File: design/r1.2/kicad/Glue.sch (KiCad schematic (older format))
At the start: 32 parts, among them IC2 ATF16V8BQL-15PU, IC3 ATF16V8BQL, IC5 ATF16V8BQL, IC6 74174N, IC8 555N, IC9 74LS01N, Q2 5H8ET-10.000, Q3 5H8ET-4.000

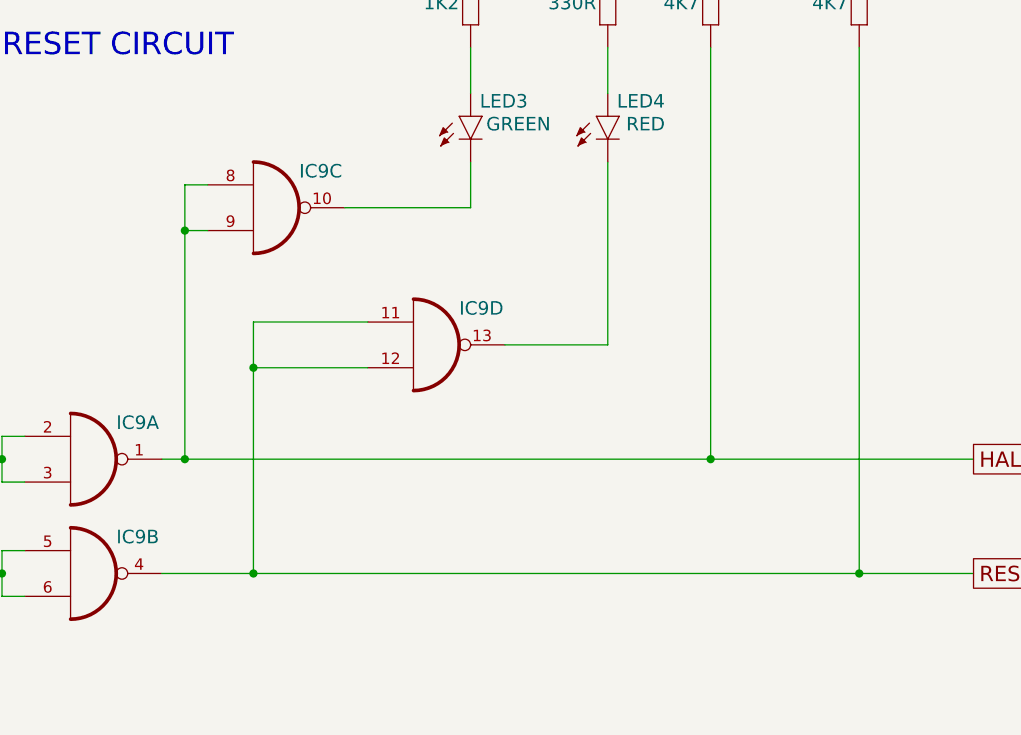
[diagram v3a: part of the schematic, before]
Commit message: Fix reset LED snafu
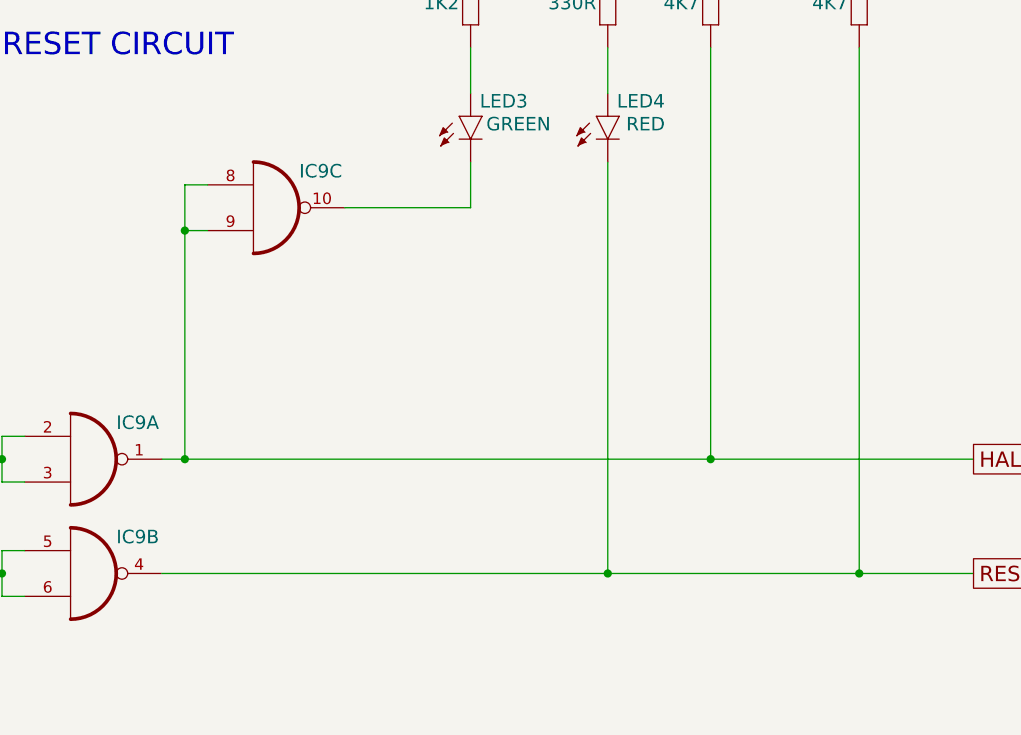
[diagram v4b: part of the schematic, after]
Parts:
- removed unit 4 of IC9
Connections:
- net RESET: now also LED3.K (C)
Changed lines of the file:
@@
 Text GLabel 3750 8500 3    70   UnSpc ~ 0
 IPL2
-$Comp
-L rosco_m68k-eagle-import:7401N IC?
-U 4 1 5ED1F8C3
-P 14000 8000
-AR Path="/5ED1F8C3" Ref="IC?"  Part="3"
-AR Path="/5E53B952/5ED1F8C3" Ref="IC9"  Part="4"
-F 0 "IC9" H 14100 8125 59  0000 L BNN
-F 1 "74LS01N" H 14100 7800 59  0001 L BNN
-F 2 "rosco_m68k:DIL14" H 14000 8000 50  0001 C CNN
-F 3 "" H 14000 8000 50  0001 C CNN
-	4    14000 8000
-	1    0    0    -1
-$EndComp
 Wire Wire Line
 	12900 7500 12900 8500
@@
 	12900 8500 15200 8500
 Connection ~ 12900 8500
-Wire Wire Line
-	12800 9000 13200 9000
-Wire Wire Line
-	13200 7900 13200 8100
-Connection ~ 13200 9000
-Connection ~ 13200 8100
-Wire Wire Line
-	13200 8100 13200 9000
-Wire Wire Line
-	14750 7200 14750 8000
-Wire Wire Line
-	13200 7900 13700 7900
-Wire Wire Line
-	13200 8100 13700 8100
-Wire Wire Line
-	14300 8000 14750 8000
 Connection ~ 15850 9000
 Wire Wire Line
 	15850 9000 16350 9000
-Wire Wire Line
-	13200 9000 15850 9000
 Wire Wire Line
 	15200 6200 15850 6200
@@
 A17
 Wire Wire Line
+	12800 9000 14750 9000
+Wire Wire Line
+	14750 7200 14750 9000
+Wire Wire Line
 	18700 6600 19700 6600
 Wire Bus Line
@@
 Wire Bus Line
 	19400 6050 19400 7500
+Connection ~ 14750 9000
+Wire Wire Line
+	14750 9000 15850 9000
 $EndSCHEMATC

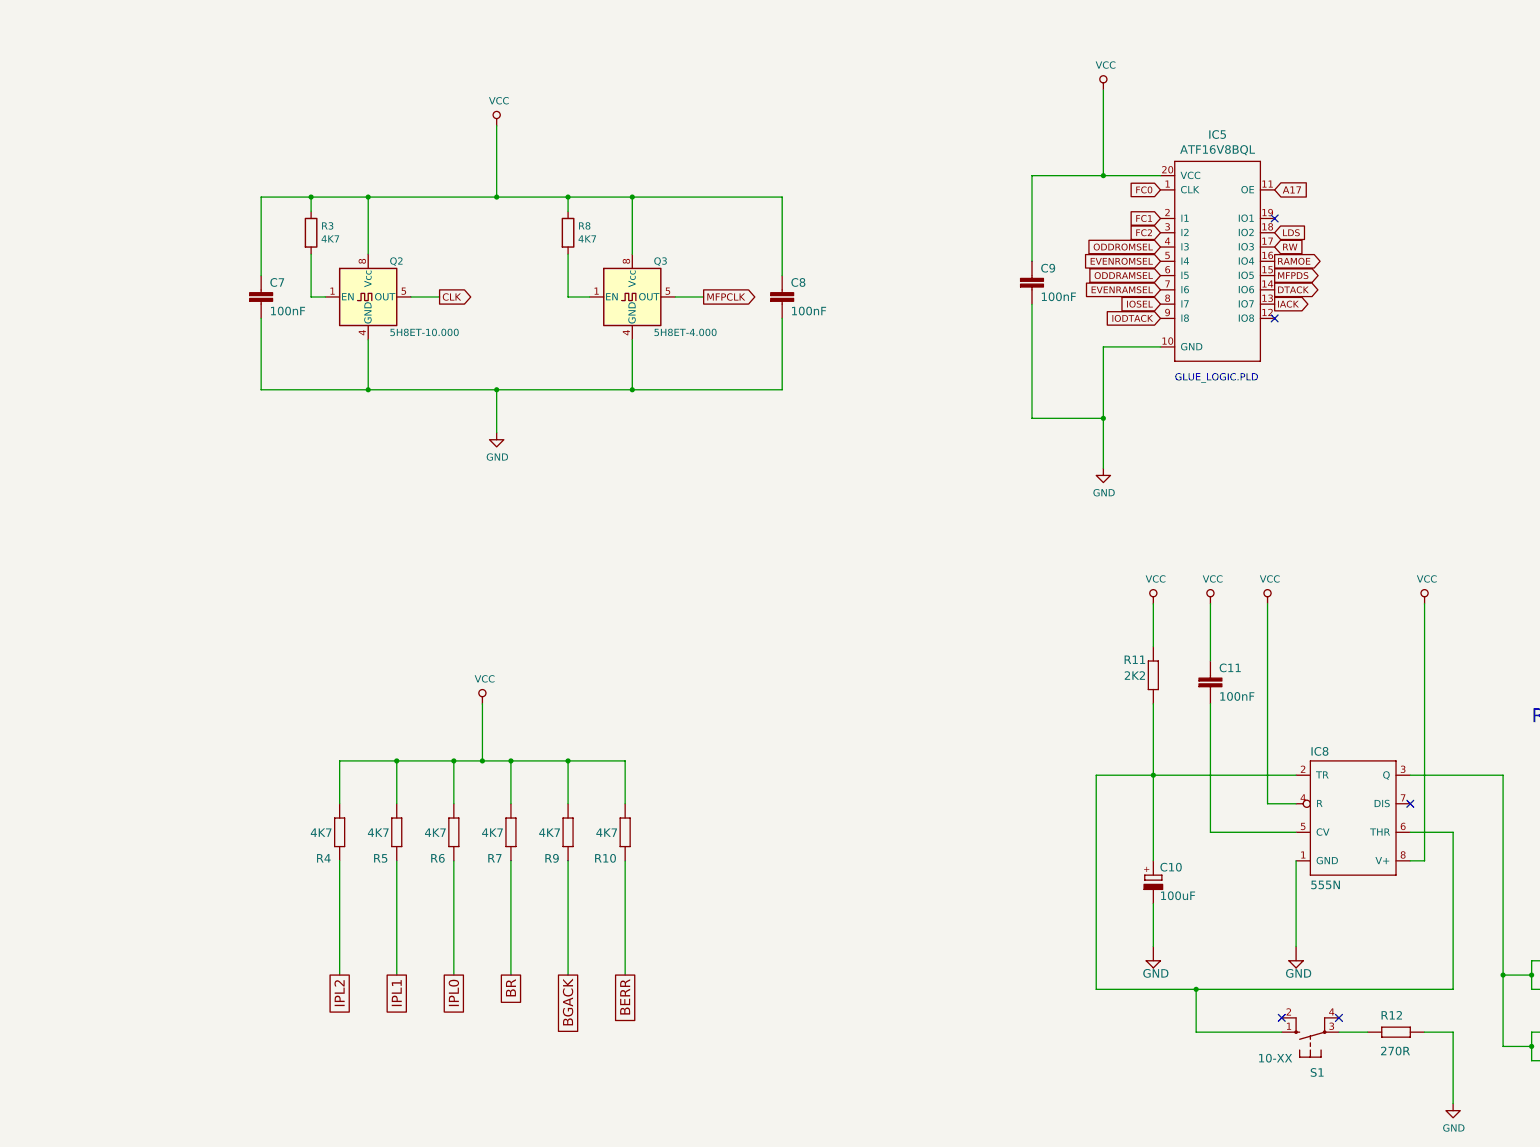
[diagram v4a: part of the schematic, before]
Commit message: Add DTACK watchdog, tidy up footprints
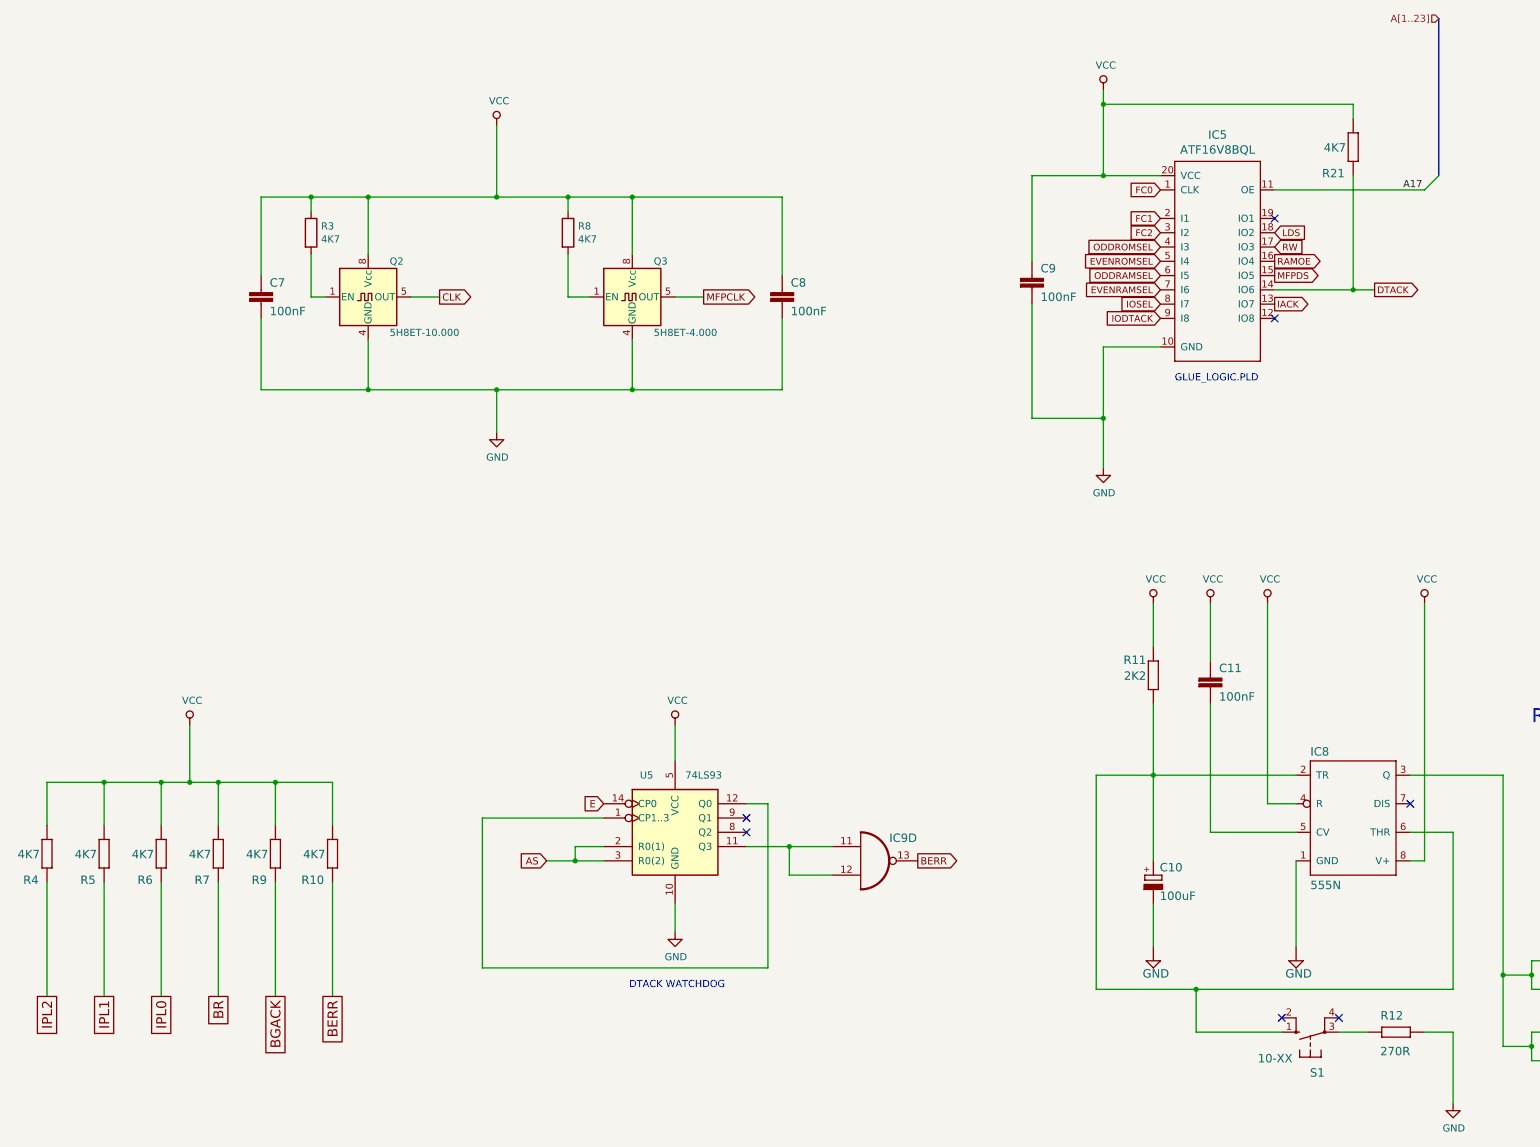
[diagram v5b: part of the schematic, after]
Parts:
- added unit 4 of IC9
- added R21: 4K7, rosco_m68k:0207_10, symbol rosco_m68k-eagle-import:R-EU_0207_10
- added U5: 74LS93, Package_DIP:DIP-14_W7.62mm_Socket_LongPads, symbol 74xx:74LS93
- IC6: footprint rosco_m68k:DIL16 -> Package_DIP:DIP-16_W7.62mm_Socket_LongPads
- IC9: footprint rosco_m68k:DIL14 -> Package_DIP:DIP-14_W7.62mm_Socket_LongPads
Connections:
- net AS: now also U5.2 (R0(1)), U5.3 (R0(2))
- net BERR: now also IC9.13 (O)
- net DTACK: now also R21.1
- net GND: now also U5.10 (GND)
- net VCC: now also R21.2, U5.5 (VCC)
- new net: U5.1 (CP1..3), U5.12 (Q0)
- new net: IC9.11 (I0), IC9.12 (I1), U5.11 (Q3)
- new net E: U5.14 (CP0)
- no-connect marks 10 -> 12
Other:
- note added: "DTACK WATCHDOG"
- moved on the sheet: R10, R4, R5, R6, R7, R9

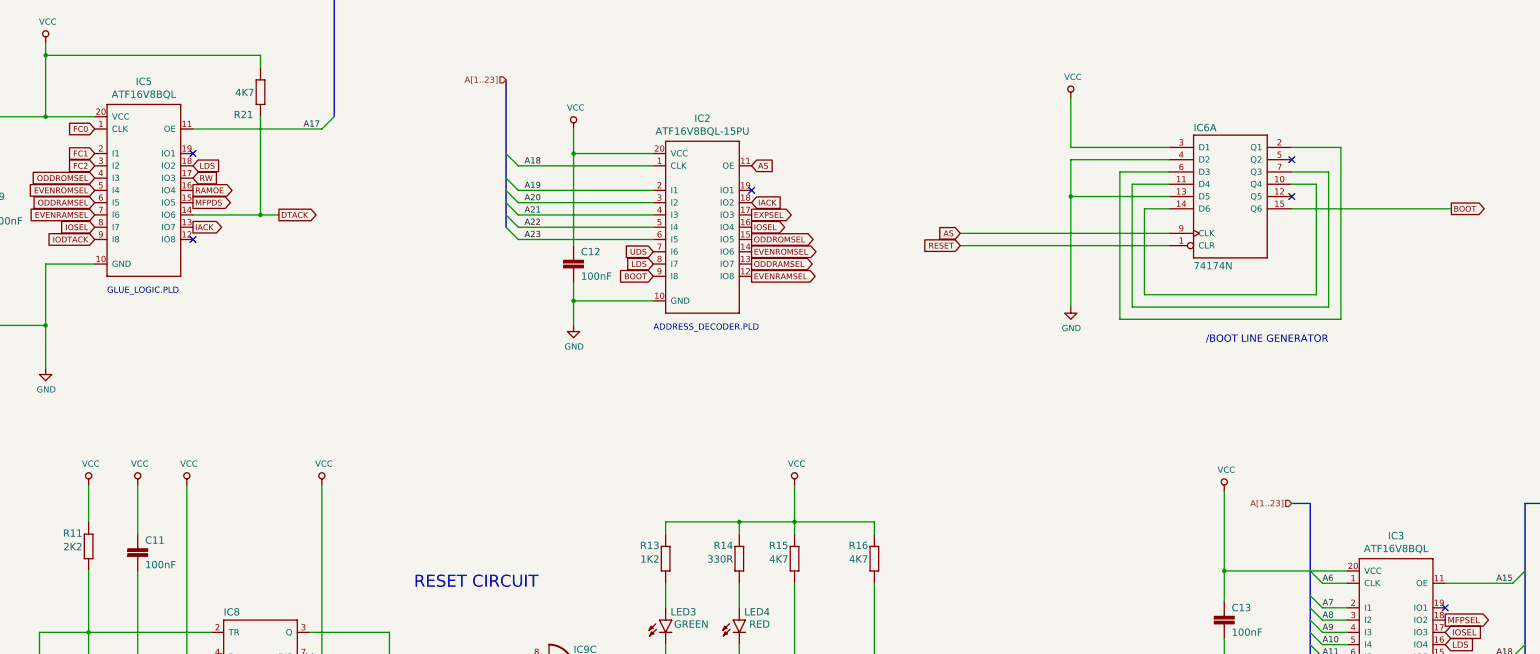
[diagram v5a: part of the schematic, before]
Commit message: Rerate LED limiters for new LED stock
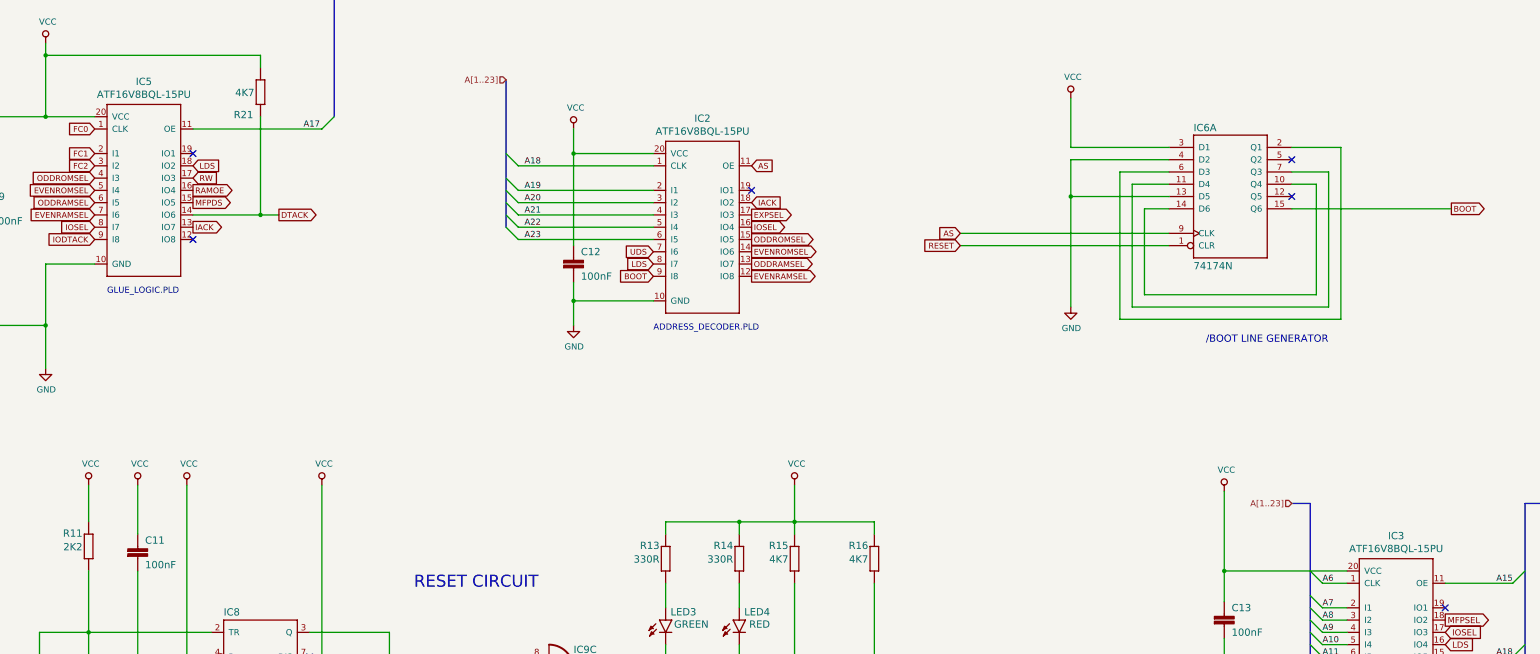
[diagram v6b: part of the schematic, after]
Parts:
- IC3, IC5: value ATF16V8BQL -> ATF16V8BQL-15PU
- R15: value 1K2 -> 330R
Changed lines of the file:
@@
 AR Path="/5E53B952/FD2CBBBB" Ref="R13"  Part="1"
 F 0 "R13" V 14291 6550 59  0000 L BNN
-F 1 "1K2" V 14180 6550 59  0000 L BNN
+F 1 "330R" V 14180 6550 59  0000 L BNN
 F 2 "rosco_m68k:0207_10" H 14150 6500 50  0001 C CNN
 F 3 "" H 14150 6500 50  0001 C CNN
@@
 AR Path="/5E53B952/5EE7D485" Ref="IC5"  Part="1"
 F 0 "IC5" H 9900 4386 59  0000 C CNN
-F 1 "ATF16V8BQL" H 9900 4281 59  0000 C CNN
+F 1 "ATF16V8BQL-15PU" H 9900 4281 59  0000 C CNN
 F 2 "rosco_m68k:DIL20" H 9900 3500 50  0001 C CNN
 F 3 "" H 9900 3500 50  0001 C CNN
@@
 AR Path="/5E53B952/5EF2F381" Ref="IC3"  Part="1"
 F 0 "IC3" H 20100 8086 59  0000 C CNN
-F 1 "ATF16V8BQL" H 20100 7981 59  0000 C CNN
+F 1 "ATF16V8BQL-15PU" H 20100 7981 59  0000 C CNN
 F 2 "rosco_m68k:DIL20" H 20100 7200 50  0001 C CNN
 F 3 "" H 20100 7200 50  0001 C CNN
@@
 Wire Wire Line
 	10300 3000 11350 3000
+Text Label 11200 3000 0    50   ~ 0
+A17
 Wire Wire Line
 	18700 6600 19700 6600
@@
 Wire Bus Line
 	19400 6050 19400 7500
-Text Label 11200 3000 0    50   ~ 0
-A17
 $EndSCHEMATC

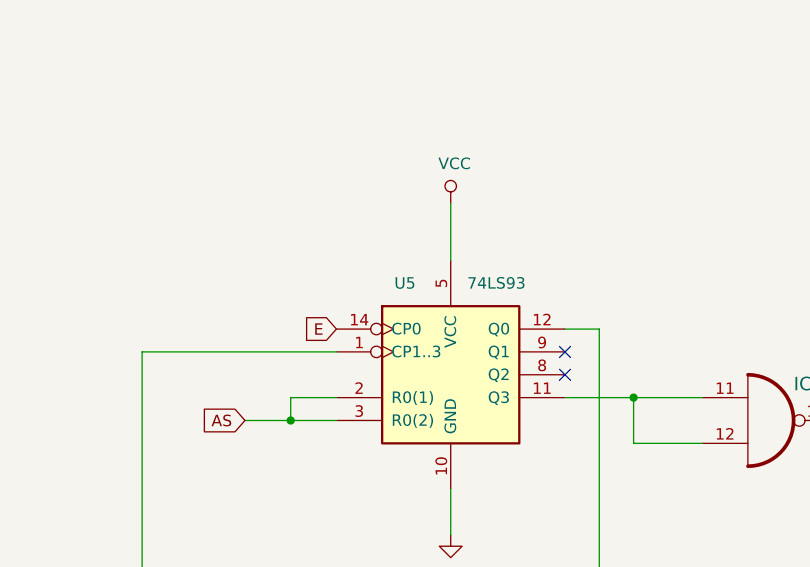
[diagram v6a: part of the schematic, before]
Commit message: Fix 1.21 incorrect IC7 ref (was U5)
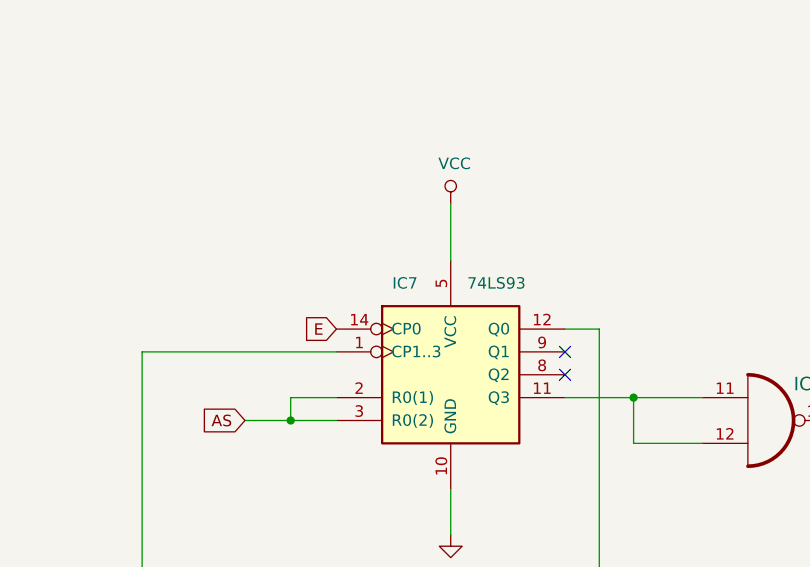
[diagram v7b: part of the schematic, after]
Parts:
- renumbered U5 to IC7
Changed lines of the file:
@@
 	10850 3700 10300 3700
 $Comp
-L 74xx:74LS93 U5
+L 74xx:74LS93 IC7
 U 1 1 5F3446CA
 P 6100 7500
-F 0 "U5" H 5900 7900 50  0000 C CNN
+F 0 "IC7" H 5900 7900 50  0000 C CNN
 F 1 "74LS93" H 6300 7900 50  0000 C CNN
 F 2 "Package_DIP:DIP-14_W7.62mm_Socket_LongPads" H 6100 7500 50  0001 C CNN
